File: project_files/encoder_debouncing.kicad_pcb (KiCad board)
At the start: 2 copper layers, 25.4 x 25.4 mm, 18 parts, among them J1 Header, J2 Header, SW1 RotaryEncoder_Switch, U1 74HC14

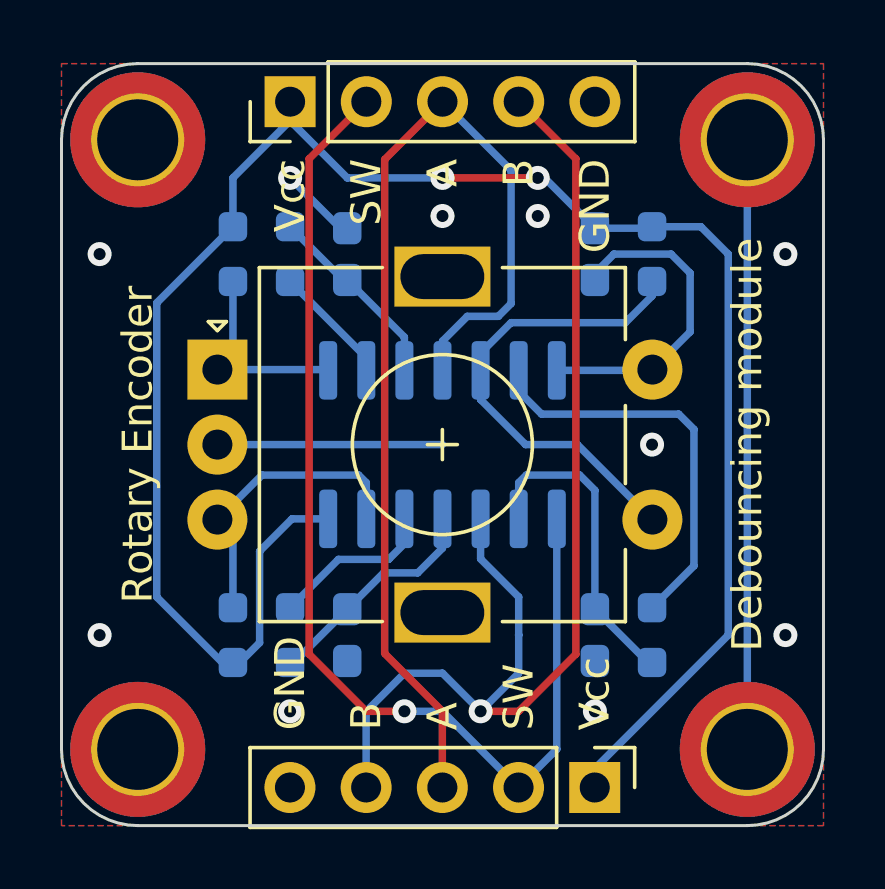
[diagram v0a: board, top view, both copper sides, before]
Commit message: correction after DRC test
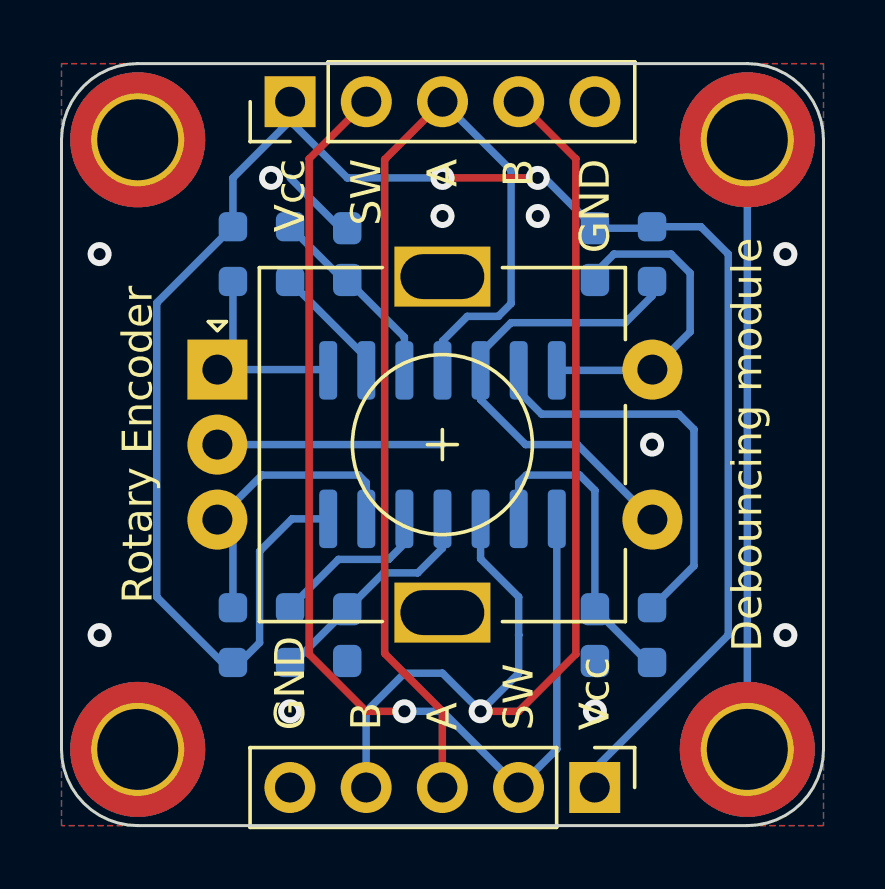
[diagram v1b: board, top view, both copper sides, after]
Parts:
- H1, H2, H3, H4: value MountingHole_Pad -> M2.5
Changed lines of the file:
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@@
-(kicad_pcb (version 20210623) (generator pcbnew)
+(kicad_pcb (version 20210424) (generator pcbnew)
   (general
     (thickness 1.6)
@@
       (effects (font (size 1 1) (thickness 0.15)))
     )
-    (fp_text value "MountingHole_Pad" (at 0 3.25) (layer "F.Fab")
+    (fp_text value "M2.5" (at 0 3.25) (layer "F.Fab")
       (effects (font (size 1 1) (thickness 0.15)))
     )
@@
       (effects (font (size 1 1) (thickness 0.15)))
     )
-    (fp_text value "MountingHole_Pad" (at 0 3.25) (layer "F.Fab")
+    (fp_text value "M2.5" (at 0 3.25) (layer "F.Fab")
       (effects (font (size 1 1) (thickness 0.15)))
     )
@@
       (effects (font (size 1 1) (thickness 0.15)))
     )
-    (fp_text value "MountingHole_Pad" (at 0 3.25) (layer "F.Fab")
+    (fp_text value "M2.5" (at 0 3.25) (layer "F.Fab")
       (effects (font (size 1 1) (thickness 0.15)))
     )
@@
       (effects (font (size 1 1) (thickness 0.15)))
     )
-    (fp_text value "MountingHole_Pad" (at 0 3.25) (layer "F.Fab")
+    (fp_text value "M2.5" (at 0 3.25) (layer "F.Fab")
       (effects (font (size 1 1) (thickness 0.15)))
     )
@@
     (fp_circle (center 0 0) (end 2.5 0) (layer "F.CrtYd") (width 0.05) (fill none))
     (pad "1" connect circle locked (at 0 0) (size 4.5 4.5) (layers "F.Cu" "F.Mask")
-      (net 2 "GND") (pinfunction "1"))
+      (net 2 "GND") (pinfunction "1") (pintype "input"))
     (pad "1" thru_hole circle locked (at 0 0) (size 3.1 3.1) (drill 2.7) (layers *.Cu *.Mask)
-      (net 2 "GND") (pinfunction "1"))
+      (net 2 "GND") (pinfunction "1") (pintype "input"))
     (pad "1" connect circle locked (at 0 0) (size 4.5 4.5) (layers "B.Cu" "B.Mask")
-      (net 2 "GND") (pinfunction "1"))
+      (net 2 "GND") (pinfunction "1") (pintype "input"))
   )
   (footprint "Resistor_SMD:R_0603_1608Metric_Pad0.98x0.95mm_HandSolder" (layer "B.Cu")
@@
   (segment (start 180.34 106.3225) (end 180.47 106.3225) (width 0.25) (layer "B.Cu") (net 1))
   (via (at 173.99 92.71) (size 0.8) (drill 0.4) (layers "F.Cu" "B.Cu") (free) (net 2))
-  (via (at 180.34 90.17) (size 0.8) (drill 0.4) (layers "F.Cu" "B.Cu") (free) (net 2))
+  (via (at 179.705 90.17) (size 0.8) (drill 0.4) (layers "F.Cu" "B.Cu") (free) (net 2))
   (via (at 180.34 107.95) (size 0.8) (drill 0.4) (layers "F.Cu" "B.Cu") (free) (net 2))
   (via (at 196.85 105.41) (size 0.8) (drill 0.4) (layers "F.Cu" "B.Cu") (free) (net 2))
@@
         (xy 172.72 111.76)
         (xy 172.72 86.36)
-        (xy 198.12 86.36)      )
+        (xy 198.12 86.36)
+      )
     )
   )
@@
         (xy 172.72 111.76)
         (xy 172.72 86.36)
-        (xy 198.12 86.36)      )
-    )
-  )
+        (xy 198.12 86.36)
+      )
+    )
+  )

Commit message: values update
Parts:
- C2, C3, C4: value 91nF -> 100nF
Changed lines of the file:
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@@
       (effects (font (size 1 1) (thickness 0.15)) (justify mirror))
     )
-    (fp_text value "91nF" (at 0 -1.43 90) (layer "B.Fab")
+    (fp_text value "100nF" (at 0 -1.43 90) (layer "B.Fab")
       (effects (font (size 1 1) (thickness 0.15)) (justify mirror))
     )
@@
       (effects (font (size 1 1) (thickness 0.15)) (justify mirror))
     )
-    (fp_text value "91nF" (at 0 -1.43 90) (layer "B.Fab")
+    (fp_text value "100nF" (at 0 -1.43 90) (layer "B.Fab")
       (effects (font (size 1 1) (thickness 0.15)) (justify mirror))
     )
@@
       (effects (font (size 1 1) (thickness 0.15)) (justify mirror))
     )
-    (fp_text value "91nF" (at 0 -1.43 90) (layer "B.Fab")
+    (fp_text value "100nF" (at 0 -1.43 90) (layer "B.Fab")
       (effects (font (size 1 1) (thickness 0.15)) (justify mirror))
     )
@@
     (pts (xy 175.26 88.9) (xy 175.26 109.22))
     (height 8.89)
-    (gr_text "0.8000 in" (at 165.22 99.06 90) (layer "Dwgs.User")
+    (gr_text "20.3200 mm" (at 165.22 99.06 90) (layer "Dwgs.User")
       (effects (font (size 1 1) (thickness 0.15)))
     )
@@
     (pts (xy 180.34 86.36) (xy 180.34 111.76))
     (height 17.78)
-    (gr_text "1.0000 in" (at 161.41 99.06 90) (layer "Dwgs.User")
+    (gr_text "25.4000 mm" (at 161.41 99.06 90) (layer "Dwgs.User")
       (effects (font (size 1 1) (thickness 0.15)))
     )
@@
     (pts (xy 172.72 88.9) (xy 198.12 88.9))
     (height -6.35)
-    (gr_text "1.0000 in" (at 185.42 81.4) (layer "Dwgs.User")
+    (gr_text "25.4000 mm" (at 185.42 81.4) (layer "Dwgs.User")
       (effects (font (size 1 1) (thickness 0.15)))
     )
@@
     (pts (xy 175.26 88.9) (xy 195.58 88.9))
     (height -4.445)
-    (gr_text "0.8000 in" (at 185.42 83.305) (layer "Dwgs.User")
+    (gr_text "20.3200 mm" (at 185.42 83.305) (layer "Dwgs.User")
       (effects (font (size 1 1) (thickness 0.15)))
     )
@@
     (pts (xy 180.34 87.63) (xy 180.34 110.49))
     (height 15.875)
-    (gr_text "0.9000 in" (at 163.315 99.06 90) (layer "Dwgs.User")
-      (effects (font (size 1 1) (thickness 0.15)))
-    )
+    (gr_text "22.8600 mm" (at 163.315 99.06 90) (layer "Dwgs.User")
+      (effects (font (size 1 1) (thickness 0.15)))
+    )
